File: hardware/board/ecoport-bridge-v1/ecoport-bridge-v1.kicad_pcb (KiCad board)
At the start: 2 copper layers, 51.5 x 92 mm, 73 parts, among them J1 420B2V12FL0, J2 Conn_01x02, J3 BM04B-SRSS-TB, J4 USB4085-GF-A, J5 Conn_01x02, J6 Connector Wire, J7 B3B-PH-K-S, SW1 RESET, SW2 BOOT, U1 IRM-05-5, U2 TLV75733PDBVR, U3 SP3485EET, U4 USBLC6-2SC6, U5 SN74LV1T34DCKR, U6 ESP32-C6-WROOM-1-N8, U7 USBLC6-2SC6, U8 LM66100DCKR

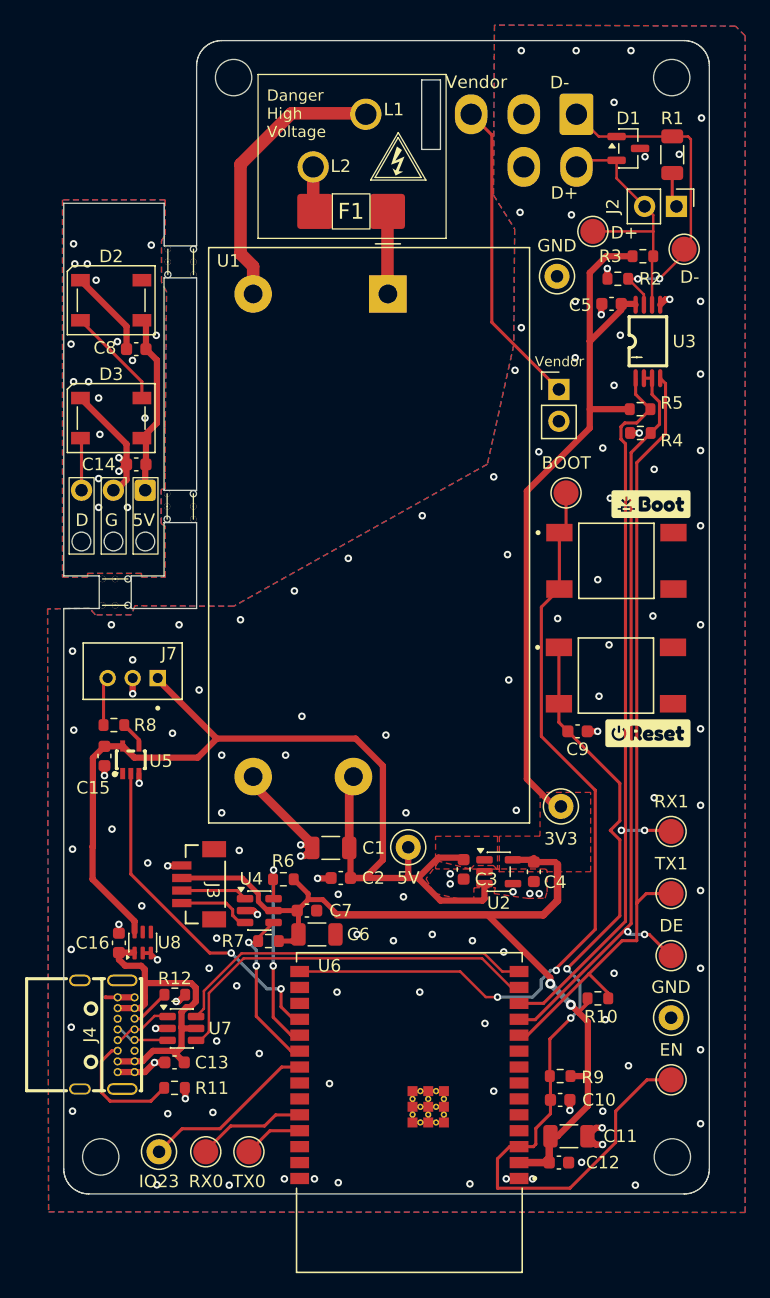
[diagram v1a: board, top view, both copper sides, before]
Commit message: Rounded traces, board edge, fixed diode traces
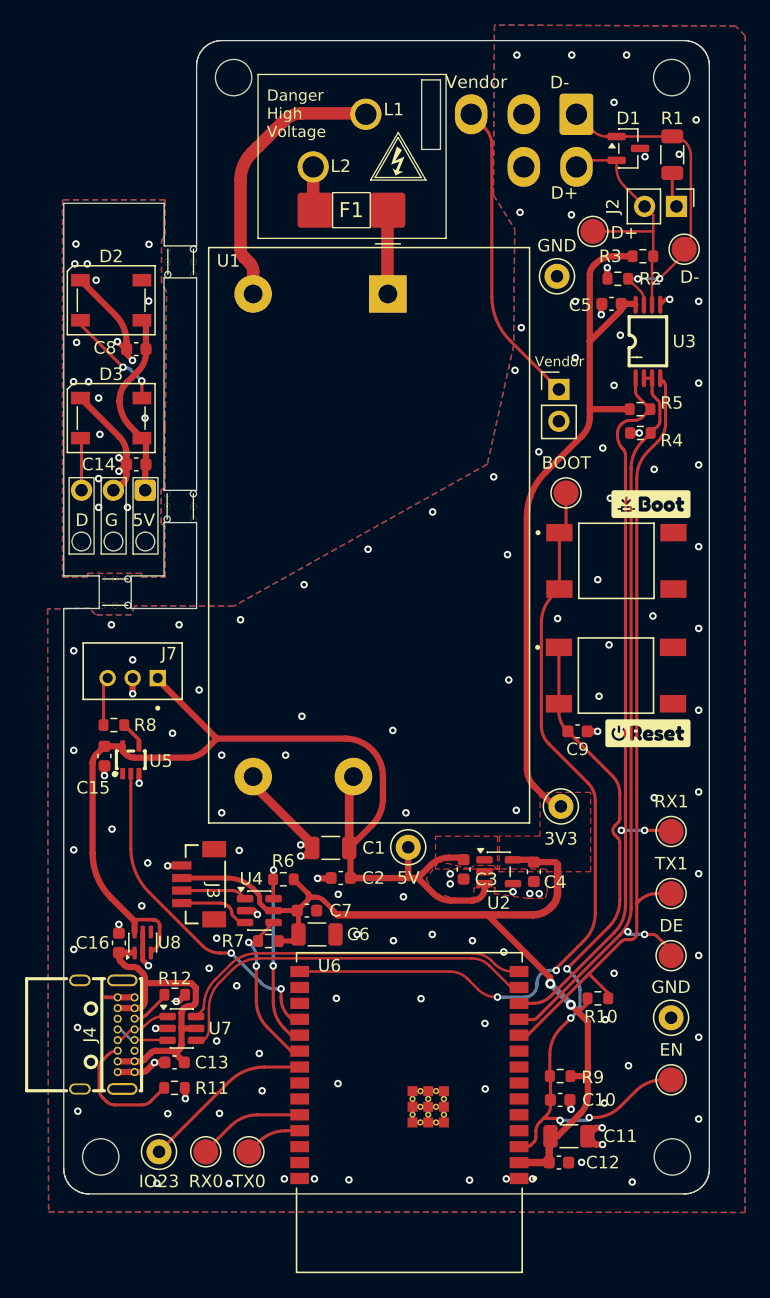
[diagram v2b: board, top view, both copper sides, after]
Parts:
- moved F1 0.10 mm to (73.4, 45.7)
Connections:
- U8 pad 3: GND -> +5V
- U8 pad 5: unconnected-(U8-ST-Pad5) -> GND
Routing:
- net /EN: track 70.7 -> 57.5 mm, vias 2 -> 4
- net +3V3: track 145.5 -> 132.6 mm
- net +5V: track 86.1 -> 87.9 mm
- net LED_GND: track 18.1 -> 19.9 mm
- net GND: track 34.3 -> 35.8 mm, vias 125 -> 126
- net /LED: track 27.6 -> 26.7 mm
- net /BOOT: track 64.6 -> 63.8 mm
- net /Data-: track 27.2 -> 26.5 mm
- net /TXD1: track 64.2 -> 63.5 mm
- net Net-(D2-DIN): track 8.23 -> 8.47 mm, vias 0 -> 2
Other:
- board text removed: "1.8"
- board text removed: "26.2"
- board text removed: "7.6"
